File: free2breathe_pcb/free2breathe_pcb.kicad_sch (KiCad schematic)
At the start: 102 parts, among them J1 USB4110-GF-A_REVB, J2 LED_Connector, J3 Alarm_Connector, Q1 AO3401A, Q2 DMN3404L, U1 IP5328, U2 MCP6044-E/P, U3 MCP6044-E/P, U4 SO2 Sensor, U5 CO Sensor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

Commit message: changed schematic to new sensor cirucit
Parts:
- removed C18, C19, C24, C25, C30, C31, C32: 0.1u, Capacitor_SMD:C_0603_1608Metric, symbol Device:C
- removed U7: O3 Sensor, components:XDCR_110-102, symbol 110-102:110-102
- removed U8: MCP6044-E/P, components:DIP254P762X533-14, symbol MCP6044-E_P:MCP6044-E/P
- added C18, C19, C24, C25: 1.0u, symbol Device:C_Polarized_US
- added R37, R38: 49.9, Resistor_SMD:R_0603_1608Metric, symbol Device:R
- added R39: 100k, Resistor_SMD:R_0603_1608Metric, symbol Device:R
- added R40: 499k, Resistor_SMD:R_0603_1608Metric, symbol Device:R
- added U7: MCP6044-E/P, components:DIP254P762X533-14, symbol MCP6044-E_P:MCP6044-E/P
- added U8: SO2 Sensor, components:XDCR_110-102, symbol 110-102:110-102
- R12: value 10 -> 2k
- R13: value 10k -> 1M
- R14, R16, R20, R21, R26, R28, R29, R31, R34, R35: value 10 -> 1M
- R15, R30: value 10 -> 16.2k
- R17: value 4.7k -> 1M
- R18, R19, R32, R33: value 10 -> 100K
- R22: value 10 -> 49.9
- R23: value 10k -> 49.9
- R24: value 910 -> 100k
- R25: value 4.7k -> 499k
- R27: value 10 -> 143k
- U4: value SO2 Sensor -> O3 Sensor
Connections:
- net Arduino_3V3: now also R26.1, U7.4 (VDD); no longer R23.1
- net Arduino_A0: now also U2.13 (VIND-), U2.14 (VOUTD), U7.13 (VIND-), U7.14 (VOUTD)
- net Arduino_A1: now also U6.13 (VIND-), U6.14 (VOUTD); no longer U3.8 (VOUTC), U3.9 (VINC-)
- net Arduino_A2: no longer U2.13 (VIND-), U2.14 (VOUTD)
- net Arduino_A3: no longer U2.8 (VOUTC), U2.9 (VINC-)
- net GND: now also R16.2, R28.2, R31.2, C18.2, C19.2, C24.2, C25.2, U7.11 (VSS); no longer C20.2, C21.2, C26.2, C28.2, R25.2
- net at U6.1 (VOUTA): now also R34.1; no longer R26.1
- net at U6.2 (VINA-): now also C28.1, U8.4 (REFERENCE)
- net at R34.2: now also U6.5 (VINB+), C24.1
- net at R29.2: now also R30.1, U7.10 (VINC+); no longer C28.1
- net at U3.1 (VOUTA): now also R20.1; no longer R14.1
- net at U3.2 (VINA-), U5.4 (REFERENCE): now also C22.1
- net at U9.1 (WORKING), U9.6 (WORKING): now also C27.1, R40.2, U7.9 (VINC-); no longer R31.1
- net at R12.1: now also R13.2, U3.3 (VINA+); no longer U2.1 (VOUTA)
- net at R12.2: now also R17.1, U3.10 (VINC+); no longer U4.5 (COUNTER)
- net at R27.1: now also R26.2, U6.3 (VINA+); no longer C27.1
- net at C27.2: now also R33.1, R40.1, U7.8 (VOUTC); no longer U9.4 (REFERENCE)
- net at R35.2: now also C25.1, U7.5 (VINB+)
- net at R32.2, U6.12 (VIND+): no longer C29.1, U6.7 (VOUTB)
- net at U2.2 (VINA-), U4.4 (REFERENCE): now also C23.1
- net at U9.5 (COUNTER): now also C29.2, R38.2; no longer R27.2
- net at R15.2, U2.3 (VINA+): now also R16.1; no longer C20.1
- net at U5.1 (WORKING), U5.6 (WORKING): now also C20.1, R24.2, U3.9 (VINC-); no longer R19.1
- net at R22.2: now also C22.2, U5.5 (COUNTER); no longer U2.5 (VINB+)
- net at R14.2: now also R15.1, U2.10 (VINC+); no longer U5.5 (COUNTER)
- net at U4.1 (WORKING), U4.6 (WORKING): now also C21.1, R25.2, U2.9 (VINC-); no longer R18.1
- net at R33.2: now also U7.12 (VIND+); no longer U6.5 (VINB+)
- removed net 1.024V: R13.2, R16.1, R17.1
- removed net Arduino_A4: A1.23 (A4), U6.13 (VIND-), U6.14 (VOUTD)
- removed net Arduino_A5: A1.24 (A5), U6.8 (VOUTC), U6.9 (VINC-)
- net Arduino_A6: no longer names the net of A1.25 (A6)
- net Arduino_A7: no longer names the net of A1.26 (A7)
- removed net Divider_High: R22.1, R23.2, R24.1, R28.1, R29.1
- removed net Divider_Low: R15.1, R24.2, R25.1, R33.1, R35.1
- new net: R30.2, R31.1, U7.3 (VINA+)
- new net: C29.1, U7.2 (VINA-), U9.4 (REFERENCE)
- new net: C21.2, R19.1, R25.1, U2.8 (VOUTC)
- new net: R19.2, U2.12 (VIND+)
- new net: R18.2, U3.12 (VIND+)
- new net: C18.1, R20.2, U3.5 (VINB+)
- new net: R22.1, U3.6 (VINB-), U3.7 (VOUTB)
- new net: C20.2, R18.1, R24.1, U3.8 (VOUTC)
- new net: C23.2, R23.2, U4.5 (COUNTER)
- new net: R37.1, U6.6 (VINB-), U6.7 (VOUTB)
- new net: C28.2, R37.2, U8.5 (COUNTER)
- new net: R35.1, U7.1 (VOUTA)
- new net: C26.2, R32.1, R39.1, U6.8 (VOUTC)
- new net: R27.2, R28.1, U6.10 (VINC+)
- new net: R23.1, U2.6 (VINB-), U2.7 (VOUTB)
- new net: C26.1, R39.2, U6.9 (VINC-), U8.1 (WORKING), U8.6 (WORKING)
- new net: R38.1, U7.6 (VINB-), U7.7 (VOUTB)
- new net: R21.1, U2.1 (VOUTA)
- new net: C19.1, R21.2, U2.5 (VINB+)
- no-connect marks 28 -> 32
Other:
- note added: "CO: 3mV"
- note added: "NO2: -25mV"
- note added: "O3: -25mV"
- note removed: "CO: 0mV"
- note removed: "CO_TP1"
- note removed: "CO_TP2"
- note removed: "NO2: -200mV"
- note removed: "NO2_TP1"
- note removed: "NO2_TP2"
- note removed: "O3: -200mV"
- note removed: "O3_TP1"
- note removed: "O3_TP2"
- note removed: "SO2_TP1"
- note removed: "SO2_TP2"
- moved on the sheet: R13, R17, U3, U5

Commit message: start layout v2
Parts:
- removed C18, C19, C24, C25: 1.0u, symbol Device:C_Polarized_US
- added C18, C19, C24, C25: 1u, Capacitor_SMD:C_0603_1608Metric, symbol Device:C
- added C30, C31, C32, C33: 0.1u, Capacitor_SMD:C_0603_1608Metric, symbol Device:C
- C15: value 22uF 16v -> 22uF 16V
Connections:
- net Arduino_3V3: now also R14.1, R29.1
- net Arduino_A0: no longer U2.13 (VIND-), U2.14 (VOUTD), U7.13 (VIND-), U7.14 (VOUTD)
- net Arduino_A2: now also U2.13 (VIND-), U2.14 (VOUTD)
- net Arduino_A3: now also U7.13 (VIND-), U7.14 (VOUTD)
- net GND: now also C18.2, C19.2, C24.2, C25.2, C30.2, C31.2, C32.2, C33.2
- net at R33.2, U7.12 (VIND+): now also C33.1
- net at R19.2, U2.12 (VIND+): now also C32.1
- net at R34.2, U6.5 (VINB+): now also C18.1
- net at R18.2, U3.12 (VIND+): now also C31.1
- net at R20.2, U3.5 (VINB+): now also C19.1
- net at R35.2, U7.5 (VINB+): now also C25.1
- net at R32.2, U6.12 (VIND+): now also C30.1
- net at R21.2, U2.5 (VINB+): now also C24.1

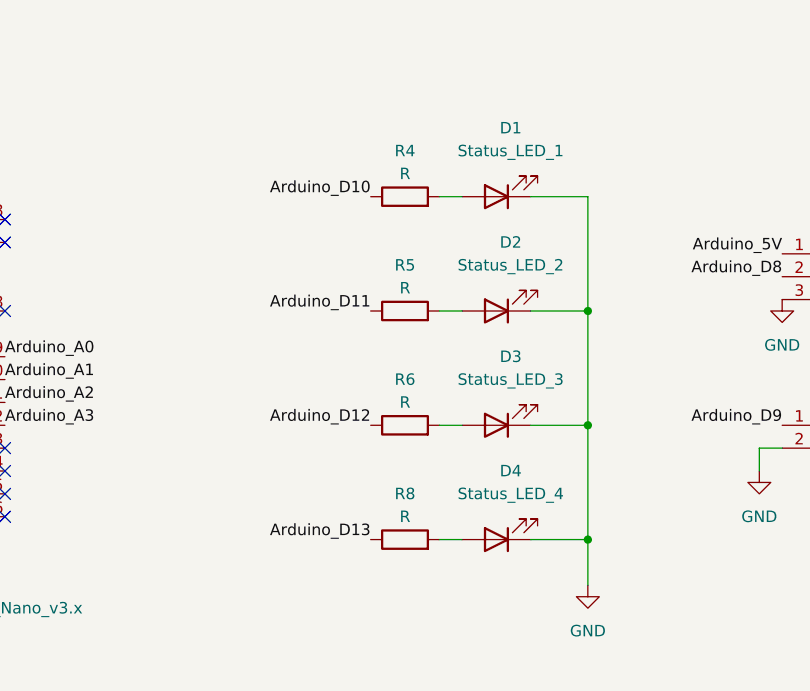
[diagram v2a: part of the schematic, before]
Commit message: changed LED resistors, placed rev2 components
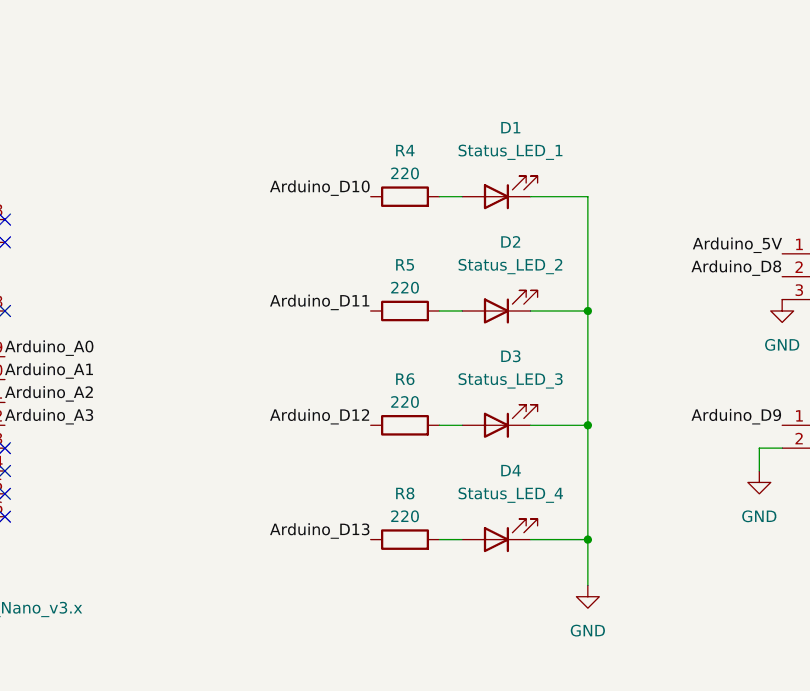
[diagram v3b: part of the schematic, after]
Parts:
- R4, R5, R6, R8: value R -> 220
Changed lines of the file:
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@@
     (in_bom yes) (on_board yes)
     (property "Reference" "R8" (id 0) (at 351.79 113.03 90))
-    (property "Value" "R" (id 1) (at 351.79 115.57 90))
+    (property "Value" "220" (id 1) (at 351.79 115.57 90))
     (property "Footprint" "Resistor_SMD:R_0603_1608Metric" (id 2) (at 351.79 119.888 90)
       (effects (font (size 1.27 1.27)) hide)
@@
     (in_bom yes) (on_board yes)
     (property "Reference" "R5" (id 0) (at 351.79 87.63 90))
-    (property "Value" "R" (id 1) (at 351.79 90.17 90))
+    (property "Value" "220" (id 1) (at 351.79 90.17 90))
     (property "Footprint" "Resistor_SMD:R_0603_1608Metric" (id 2) (at 351.79 94.488 90)
       (effects (font (size 1.27 1.27)) hide)
@@
     (in_bom yes) (on_board yes)
     (property "Reference" "R6" (id 0) (at 351.79 100.33 90))
-    (property "Value" "R" (id 1) (at 351.79 102.87 90))
+    (property "Value" "220" (id 1) (at 351.79 102.87 90))
     (property "Footprint" "Resistor_SMD:R_0603_1608Metric" (id 2) (at 351.79 107.188 90)
       (effects (font (size 1.27 1.27)) hide)
@@
     (in_bom yes) (on_board yes)
     (property "Reference" "R4" (id 0) (at 351.79 74.93 90))
-    (property "Value" "R" (id 1) (at 351.79 77.47 90))
+    (property "Value" "220" (id 1) (at 351.79 77.47 90))
     (property "Footprint" "Resistor_SMD:R_0603_1608Metric" (id 2) (at 351.79 81.788 90)
       (effects (font (size 1.27 1.27)) hide)
@@
     )
     (path "/edbbc38b-a89b-4e95-bd20-a490d6d79c74"
-      (reference "R4") (unit 1) (value "R") (footprint "Resistor_SMD:R_0603_1608Metric")
+      (reference "R4") (unit 1) (value "220") (footprint "Resistor_SMD:R_0603_1608Metric")
     )
     (path "/7fb61806-79ca-4749-8fca-a1ada20caa2c"
-      (reference "R5") (unit 1) (value "R") (footprint "Resistor_SMD:R_0603_1608Metric")
+      (reference "R5") (unit 1) (value "220") (footprint "Resistor_SMD:R_0603_1608Metric")
     )
     (path "/d07553bb-e236-4836-9c0b-23372ea41e06"
-      (reference "R6") (unit 1) (value "R") (footprint "Resistor_SMD:R_0603_1608Metric")
+      (reference "R6") (unit 1) (value "220") (footprint "Resistor_SMD:R_0603_1608Metric")
     )
     (path "/90fbf547-ea71-46d9-862e-06cd7cbcc56d"
@@
     )
     (path "/381c45d7-4d2b-43a7-aa71-f98ac50e463d"
-      (reference "R8") (unit 1) (value "R") (footprint "Resistor_SMD:R_0603_1608Metric")
+      (reference "R8") (unit 1) (value "220") (footprint "Resistor_SMD:R_0603_1608Metric")
     )
     (path "/14363a6a-8a54-4523-b848-84e100f60191"

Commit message: update board, todo, components
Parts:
- added J4: Conn_01x02_Female, switch:switch_pad, symbol Connector:Conn_01x02_Female
- added R41: 10, Resistor_SMD:R_0603_1608Metric, symbol Device:R
- added R42: 100k, Resistor_SMD:R_0603_1608Metric, symbol Device:R
- added TH2: 100k@25c, Resistor_SMD:R_0805_2012Metric, symbol Device:Thermistor
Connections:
- net Arduino_5V: now also R42.1
- net Arduino_D9: now also R41.1; no longer J3.1 (Pin_1)
- net GND: now also J4.2 (Pin_2), TH2.2
- net VOUT: now also J4.1 (Pin_1)
- net Arduino_A4: now reaches A1.23 (A4)
- net Arduino_A4: now also R42.2, TH2.1
- new net: J3.1 (Pin_1), R41.2
- no-connect marks 32 -> 31
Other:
- note added: "Power System"
- note added: "Power Test/Solder Point"
- note added: "System Temp Monitor Thermistor"
- note added: "USB-C Port"
- moved on the sheet: J3

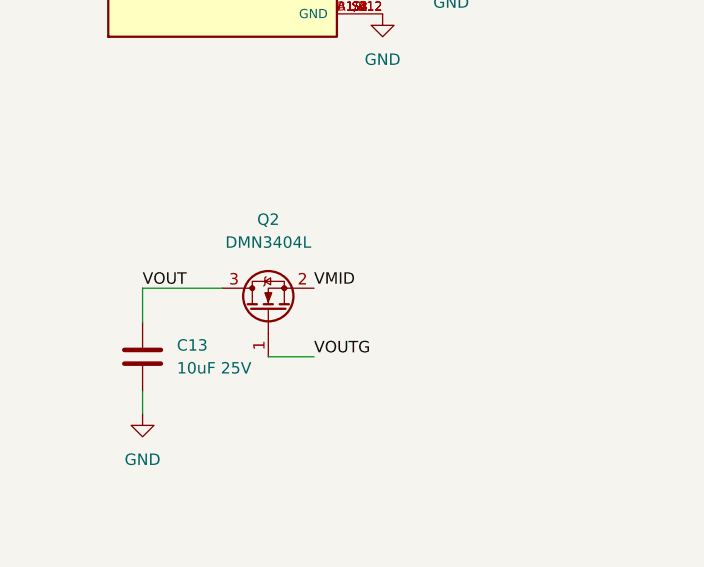
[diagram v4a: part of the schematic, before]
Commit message: update schematic for proper x-istor placement, software for testing rev. 2
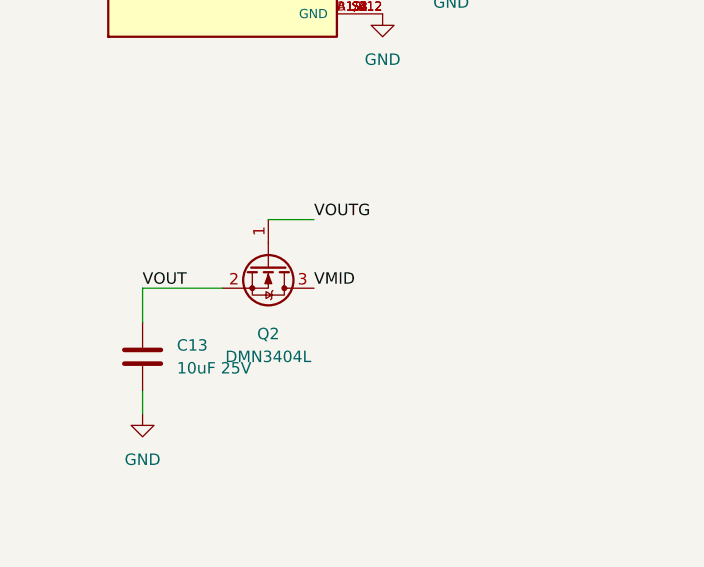
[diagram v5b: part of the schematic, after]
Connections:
- net VMID: now also Q2.3 (D); no longer Q2.2 (S)
- net VOUT: now also Q2.2 (S); no longer Q2.3 (D)
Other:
- moved on the sheet: Q2
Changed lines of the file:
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@@
     (stroke (width 0) (type default) (color 0 0 0 0))
   )
-  (wire (pts (xy 57.15 101.6) (xy 62.23 101.6))
+  (wire (pts (xy 57.15 86.36) (xy 62.23 86.36))
     (stroke (width 0) (type default) (color 0 0 0 0))
   )
@@
     (effects (font (size 1.27 1.27)) (justify right bottom))
   )
-  (label "VOUTG" (at 62.23 101.6 0)
+  (label "VOUTG" (at 62.23 86.36 0)
     (effects (font (size 1.27 1.27)) (justify left bottom))
   )
@@
     (pin "2")
   )
-  (symbol (lib_id "Transistor_FET:DMN3404L") (at 57.15 96.52 90) (unit 1)
+  (symbol (lib_id "Transistor_FET:DMN3404L") (at 57.15 91.44 270) (unit 1)
     (in_bom yes) (on_board yes) (fields_autoplaced)
-    (property "Reference" "Q2" (id 0) (at 57.15 86.36 90))
-    (property "Value" "DMN3404L" (id 1) (at 57.15 88.9 90))
-    (property "Footprint" "Package_TO_SOT_SMD:SOT-23" (id 2) (at 59.055 91.44 0)
+    (property "Reference" "Q2" (id 0) (at 57.15 99.06 90))
+    (property "Value" "DMN3404L" (id 1) (at 57.15 101.6 90))
+    (property "Footprint" "Package_TO_SOT_SMD:SOT-23" (id 2) (at 55.245 96.52 0)
       (effects (font (size 1.27 1.27) italic) (justify left) hide)
     )
-    (property "Datasheet" "http://www.diodes.com/assets/Datasheets/ds31787.pdf" (id 3) (at 57.15 96.52 0)
+    (property "Datasheet" "http://www.diodes.com/assets/Datasheets/ds31787.pdf" (id 3) (at 57.15 91.44 0)
       (effects (font (size 1.27 1.27)) (justify left) hide)
     )
